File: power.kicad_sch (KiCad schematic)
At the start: 66 parts, among them J1 USB_C_Receptacle, J3 PD controller EEPROM programm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, U1 TVS2200DRV, U10 TPS65283-1RGER, U5 CAT24C256, U6 TPS25750DRJKT, U7 PAC1951-1

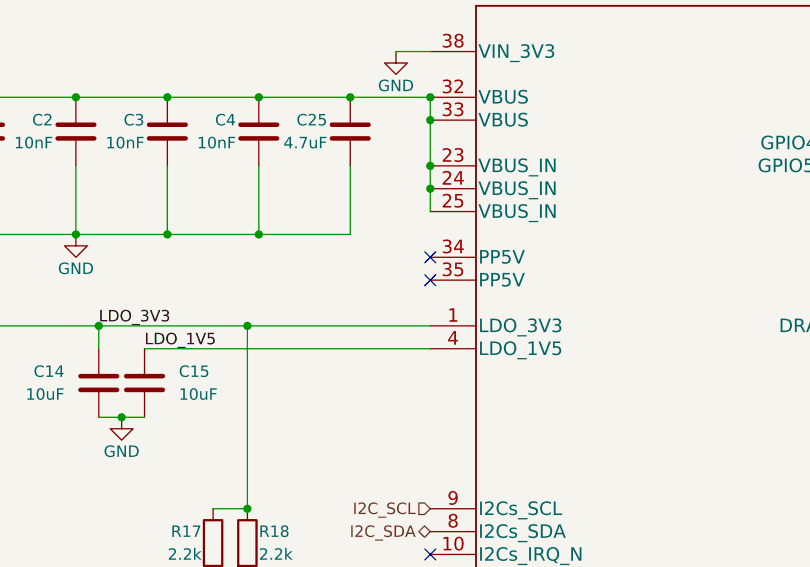
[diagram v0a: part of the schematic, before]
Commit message: Add bus debug test points
For easier debugging the I2C and SPI bus are being branched to via test
pads. Some enhancements to the PD controller are made by connecting PP5V
to ground. Also corrects the footprint of the energy meter.
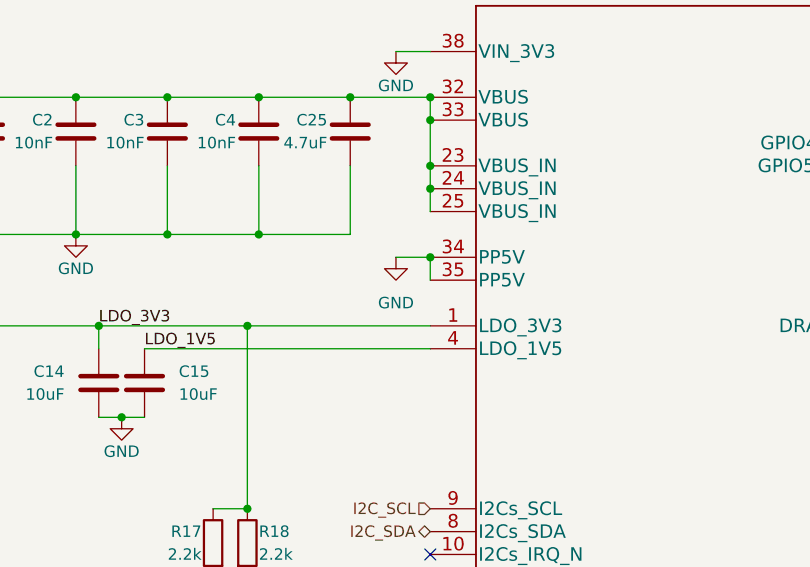
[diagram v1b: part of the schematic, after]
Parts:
- U7: footprint Package_DFN_QFN:UQFN-16-1EP_4x4mm_P0.65mm_EP2.7x2.7mm -> Package_DFN_QFN:VQFN-16-1EP_3x3mm_P0.5mm_EP1.1x1.1mm_ThermalVias
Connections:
- net GND: now also U6.34 (PP5V), U6.35 (PP5V)
- no-connect marks 27 -> 25
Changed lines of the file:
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@@
   (junction (at 227.33 91.44) (diameter 0) (color 0 0 0 0)
+  )
+  (junction (at 86.36 130.81) (diameter 0) (color 0 0 0 0)
   )
   (junction (at 180.34 36.83) (diameter 0) (color 0 0 0 0)
@@
   (no_connect (at 142.24 118.11))
   (no_connect (at 142.24 120.65))
-  (no_connect (at 86.36 133.35))
-  (no_connect (at 86.36 130.81))
   (no_connect (at 44.45 71.12))
   (no_connect (at 44.45 73.66))
@@
     (stroke (width 0) (type default) (color 0 0 0 0))
   )
+  (wire (pts (xy 86.36 130.81) (xy 86.36 133.35))
+    (stroke (width 0) (type default) (color 0 0 0 0))
+  )
   (wire (pts (xy 217.17 41.91) (xy 207.01 41.91))
     (stroke (width 0) (type default) (color 0 0 0 0))
@@
   )
   (wire (pts (xy 36.83 120.65) (xy 36.83 128.27))
+    (stroke (width 0) (type default) (color 0 0 0 0))
+  )
+  (wire (pts (xy 82.55 130.81) (xy 86.36 130.81))
     (stroke (width 0) (type default) (color 0 0 0 0))
   )
@@
     (pin "2")
   )
+  (symbol (lib_id "power:GND") (at 82.55 130.81 0) (unit 1)
+    (in_bom yes) (on_board yes) (fields_autoplaced)
+    (property "Reference" "#PWR0184" (id 0) (at 82.55 137.16 0)
+      (effects (font (size 1.27 1.27)) hide)
+    )
+    (property "Value" "GND" (id 1) (at 82.55 135.89 0))
+    (property "Footprint" "" (id 2) (at 82.55 130.81 0)
+      (effects (font (size 1.27 1.27)) hide)
+    )
+    (property "Datasheet" "" (id 3) (at 82.55 130.81 0)
+      (effects (font (size 1.27 1.27)) hide)
+    )
+    (pin "1")
+  )
   (symbol (lib_id "Device:C") (at 207.01 45.72 0) (unit 1)
     (in_bom yes) (on_board yes)
@@
       (effects (font (size 1.27 1.27)) (justify left))
     )
-    (property "Footprint" "Package_DFN_QFN:UQFN-16-1EP_4x4mm_P0.65mm_EP2.7x2.7mm" (id 2) (at 44.45 73.66 0)
-      (effects (font (size 1.27 1.27)) hide)
-    )
+    (property "Footprint" "Package_DFN_QFN:VQFN-16-1EP_3x3mm_P0.5mm_EP1.1x1.1mm_ThermalVias" (id 2) (at 44.45 73.66 0)
+      (effects (font (size 1.27 1.27)) hide)
+    )
